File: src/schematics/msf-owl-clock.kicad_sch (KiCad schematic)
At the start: 38 parts, among them U001 BC805M

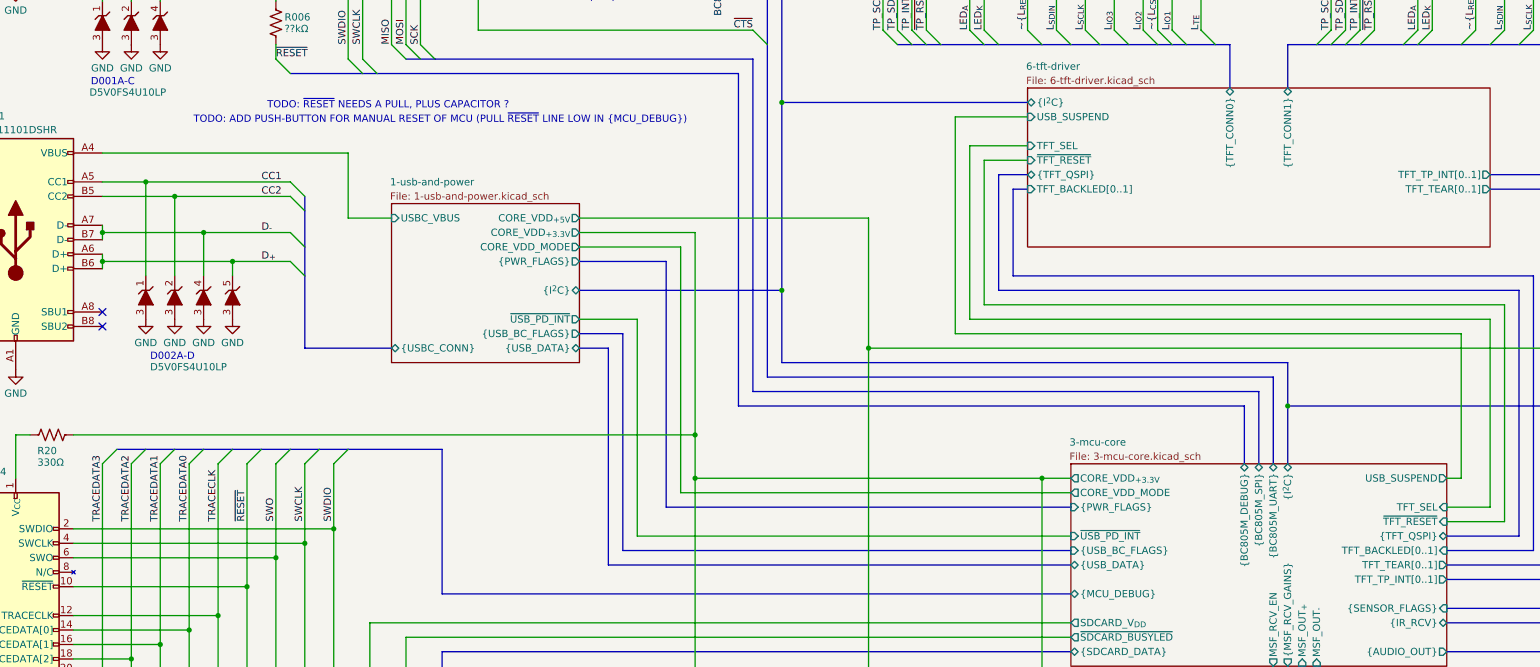
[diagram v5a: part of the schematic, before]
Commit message: Further elaboration of the USB / Power schematic.
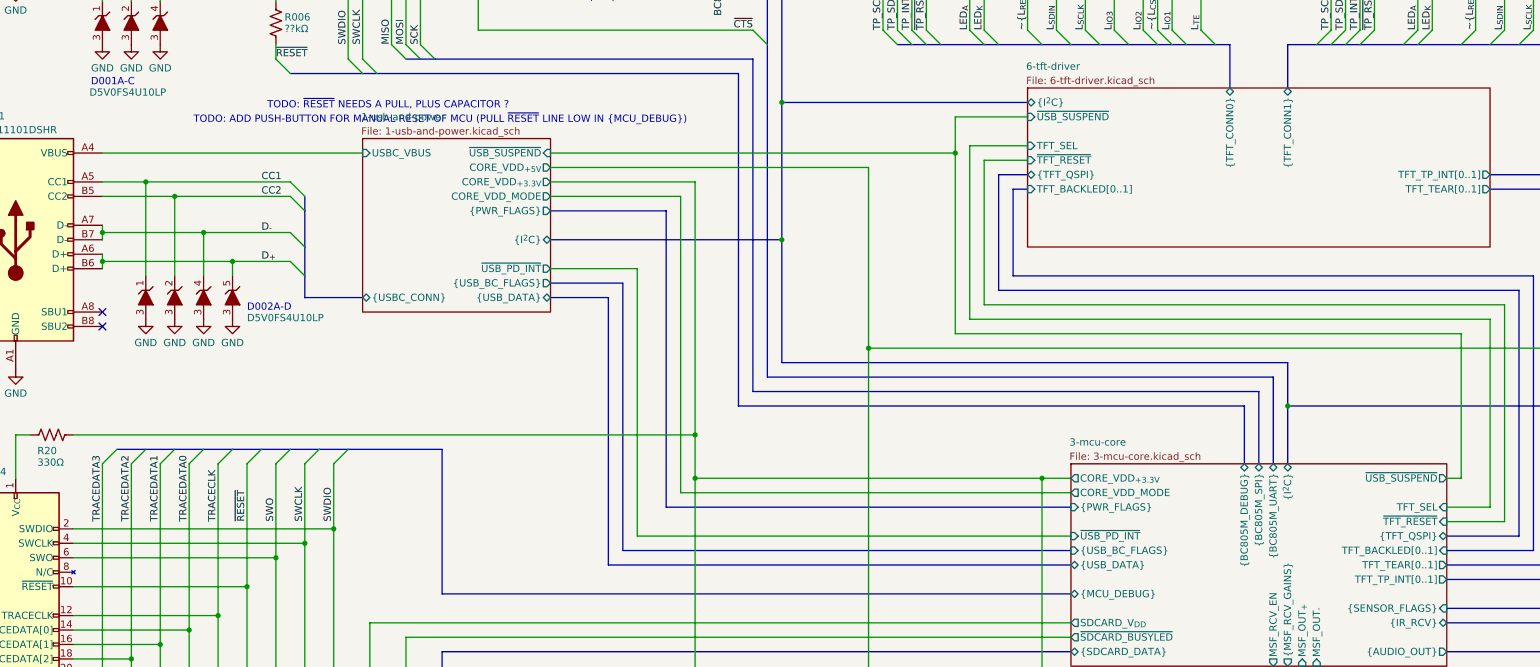
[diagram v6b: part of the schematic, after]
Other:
- sheet 1-usb-and-power ports: added ~{USB_SUSPEND}; removed none
- sheet 3-mcu-core ports: added ~{USB_SUSPEND}; removed USB_SUSPEND
- sheet 6-tft-driver ports: added ~{USB_SUSPEND}; removed USB_SUSPEND
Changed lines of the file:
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@@
   (bus_alias "TFT_CONN1" (members "TP_SCL" "TP_SDA" "TP_INT" "~{TP_{RST}}" "LED_{A}" "LED_{K}" "~{L_{RES}}" "L_{SDIN}" "L_{SCLK}" "L_{IO[1..3]}" "~{L_{CS}}" "L_{TE}"))
   (bus_alias "USBC_CONN" (members "CC[1..2]" "D_{+}" "D_{-}" "SBU[1..2]"))
-  (bus_alias "USB_BC_FLAGS" (members "~{CHARGING_ALLOWED}" "CHARGER_DETECTED" "~{NO_DATA}"))
+  (bus_alias "USB_BC_FLAGS" (members "~{CHARGING_ALLOWED}" "~{CHARGER_DETECTED}" "~{HAS_DATA}"))
   (junction (at 66.04 90.17) (diameter 0) (color 0 0 0 0)
   )
   (junction (at 73.66 163.83) (diameter 0) (color 0 0 0 0)
   )
+  (junction (at 172.72 97.79) (diameter 0) (color 0 0 0 0)
+  )
   (junction (at 81.28 215.9) (diameter 0) (color 0 0 0 0)
   )
@@
   (junction (at 58.42 35.56) (diameter 0) (color 0 0 0 0)
   )
-  (junction (at 172.72 106.68) (diameter 0) (color 0 0 0 0)
+  (junction (at 203.2 82.55) (diameter 0) (color 0 0 0 0)
   )
   (junction (at 187.96 116.84) (diameter 0) (color 0 0 0 0)
@@
     (stroke (width 0) (type default))
   )
-  (wire (pts (xy 53.34 82.55) (xy 96.52 82.55))
-    (stroke (width 0) (type default))
-  )
   (bus (pts (xy 113.03 208.28) (xy 113.03 213.36))
     (stroke (width 0) (type default))
@@
     (stroke (width 0) (type default))
   )
-  (bus (pts (xy 172.72 106.68) (xy 172.72 119.38))
-    (stroke (width 0) (type default))
-  )
   (wire (pts (xy 88.9 137.16) (xy 88.9 151.13))
     (stroke (width 0) (type default))
@@
     (stroke (width 0) (type default))
   )
+  (wire (pts (xy 203.2 82.55) (xy 203.2 76.2))
+    (stroke (width 0) (type default))
+  )
   (wire (pts (xy 96.52 33.02) (xy 127 33.02))
     (stroke (width 0) (type default))
@@
     (stroke (width 0) (type default))
   )
+  (bus (pts (xy 172.72 97.79) (xy 172.72 119.38))
+    (stroke (width 0) (type default))
+  )
   (wire (pts (xy 274.32 48.26) (xy 274.32 60.96))
     (stroke (width 0) (type default))
@@
     (stroke (width 0) (type default))
   )
+  (wire (pts (xy 132.08 82.55) (xy 203.2 82.55))
+    (stroke (width 0) (type default))
+  )
   (wire (pts (xy 83.82 137.16) (xy 83.82 153.67))
     (stroke (width 0) (type default))
@@
     (stroke (width 0) (type default))
   )
-  (wire (pts (xy 147.32 111.76) (xy 147.32 149.86))
+  (wire (pts (xy 147.32 102.87) (xy 147.32 149.86))
     (stroke (width 0) (type default))
   )
@@
     (stroke (width 0) (type default))
   )
-  (bus (pts (xy 172.72 73.66) (xy 172.72 106.68))
+  (bus (pts (xy 172.72 73.66) (xy 172.72 97.79))
     (stroke (width 0) (type default))
   )
@@
     (stroke (width 0) (type default))
   )
-  (wire (pts (xy 187.96 93.98) (xy 187.96 116.84))
+  (wire (pts (xy 187.96 85.09) (xy 187.96 116.84))
     (stroke (width 0) (type default))
   )
@@
     (stroke (width 0) (type default))
   )
-  (wire (pts (xy 154.94 142.24) (xy 154.94 99.06))
+  (wire (pts (xy 154.94 142.24) (xy 154.94 90.17))
     (stroke (width 0) (type default))
   )
@@
     (stroke (width 0) (type default))
   )
-  (bus (pts (xy 142.24 116.84) (xy 137.16 116.84))
+  (bus (pts (xy 142.24 107.95) (xy 132.08 107.95))
     (stroke (width 0) (type default))
   )
@@
     (stroke (width 0) (type default))
   )
-  (bus (pts (xy 142.24 154.94) (xy 142.24 116.84))
+  (bus (pts (xy 142.24 154.94) (xy 142.24 107.95))
     (stroke (width 0) (type default))
   )
@@
     (stroke (width 0) (type default))
   )
-  (bus (pts (xy 88.9 104.14) (xy 88.9 116.84))
-    (stroke (width 0) (type default))
-  )
   (wire (pts (xy 38.1 22.86) (xy 38.1 15.24))
     (stroke (width 0) (type default))
@@
     (stroke (width 0) (type default))
   )
-  (wire (pts (xy 137.16 96.52) (xy 157.48 96.52))
+  (wire (pts (xy 132.08 87.63) (xy 157.48 87.63))
     (stroke (width 0) (type default))
   )
@@
     (stroke (width 0) (type default))
   )
-  (wire (pts (xy 157.48 96.52) (xy 157.48 132.08))
+  (wire (pts (xy 157.48 87.63) (xy 157.48 132.08))
     (stroke (width 0) (type default))
   )
@@
     (stroke (width 0) (type default))
   )
-  (bus (pts (xy 137.16 106.68) (xy 172.72 106.68))
+  (bus (pts (xy 132.08 97.79) (xy 172.72 97.79))
     (stroke (width 0) (type default))
   )
@@
     (stroke (width 0) (type default))
   )
-  (bus (pts (xy 137.16 101.6) (xy 152.4 101.6))
+  (bus (pts (xy 132.08 92.71) (xy 152.4 92.71))
     (stroke (width 0) (type default))
   )
@@
     (stroke (width 0) (type default))
   )
+  (bus (pts (xy 88.9 104.14) (xy 88.9 107.95))
+    (stroke (width 0) (type default))
+  )
   (wire (pts (xy 167.64 60.96) (xy 119.38 60.96))
     (stroke (width 0) (type default))
@@
     (stroke (width 0) (type default))
   )
-  (wire (pts (xy 203.2 114.3) (xy 203.2 76.2))
+  (wire (pts (xy 203.2 114.3) (xy 203.2 82.55))
     (stroke (width 0) (type default))
   )
@@
     (stroke (width 0) (type default))
   )
-  (bus (pts (xy 137.16 114.3) (xy 144.78 114.3))
+  (bus (pts (xy 132.08 105.41) (xy 144.78 105.41))
     (stroke (width 0) (type default))
   )
@@
     (stroke (width 0) (type default))
   )
-  (wire (pts (xy 96.52 93.98) (xy 104.14 93.98))
+  (wire (pts (xy 53.34 82.55) (xy 99.06 82.55))
     (stroke (width 0) (type default))
   )
@@
     (stroke (width 0) (type default))
   )
-  (wire (pts (xy 96.52 82.55) (xy 96.52 93.98))
-    (stroke (width 0) (type default))
-  )
   (bus (pts (xy 113.03 160.02) (xy 113.03 134.62))
     (stroke (width 0) (type default))
@@
     (stroke (width 0) (type default))
   )
-  (wire (pts (xy 137.16 111.76) (xy 147.32 111.76))
+  (wire (pts (xy 132.08 102.87) (xy 147.32 102.87))
     (stroke (width 0) (type default))
   )
-  (wire (pts (xy 137.16 93.98) (xy 187.96 93.98))
+  (wire (pts (xy 132.08 85.09) (xy 187.96 85.09))
     (stroke (width 0) (type default))
   )
@@
     (stroke (width 0) (type default))
   )
-  (bus (pts (xy 144.78 152.4) (xy 144.78 114.3))
+  (bus (pts (xy 144.78 152.4) (xy 144.78 105.41))
     (stroke (width 0) (type default))
   )
@@
     (stroke (width 0) (type default))
   )
-  (bus (pts (xy 88.9 116.84) (xy 104.14 116.84))
+  (bus (pts (xy 88.9 107.95) (xy 99.06 107.95))
     (stroke (width 0) (type default))
   )
@@
     (stroke (width 0) (type default))
   )
-  (wire (pts (xy 154.94 99.06) (xy 137.16 99.06))
+  (wire (pts (xy 154.94 90.17) (xy 132.08 90.17))
     (stroke (width 0) (type default))
   )
@@
     (stroke (width 0) (type default))
   )
-  (bus (pts (xy 152.4 101.6) (xy 152.4 144.78))
+  (bus (pts (xy 152.4 92.71) (xy 152.4 144.78))
     (stroke (width 0) (type default))
   )
@@
     (effects (font (size 1.27 1.27)) (justify left bottom))
   )
-  (text "D002A-D" (at 61.722 119.126 0)
+  (text "D002A-D" (at 78.74 110.49 0)
     (effects (font (size 1.27 1.27)) (justify left bottom))
   )
@@
       (effects (font (size 1.27 1.27)) (justify right) hide)
     )
-    (property "Value" "D5V0FS4U10LP" (at 61.722 120.142 90)
+    (property "Value" "D5V0FS4U10LP" (at 78.74 111.506 90)
       (effects (font (size 1.27 1.27)) (justify right))
     )
@@
       (effects (font (size 1.27 1.27)) (justify right))
     )
-    (pin "USB_SUSPEND" input (at 215.9 76.2 180)
+    (pin "~{USB_SUSPEND}" input (at 215.9 76.2 180)
       (effects (font (size 1.27 1.27)) (justify left))
     )
@@
     )
   )
-  (sheet (at 104.14 91.44) (size 33.02 27.94)
+  (sheet (at 99.06 80.01) (size 33.02 30.48)
     (stroke (width 0.1524) (type solid))
     (fill (color 0 0 0 0.0000))
-    (property "Sheetname" "1-usb-and-power" (at 103.886 88.392 0)
+    (property "Sheetname" "1-usb-and-power" (at 98.806 76.962 0)
       (effects (font (size 1.27 1.27)) (justify left bottom))
     )
-    (property "Sheetfile" "1-usb-and-power.kicad_sch" (at 103.886 89.408 0)
+    (property "Sheetfile" "1-usb-and-power.kicad_sch" (at 98.806 77.978 0)
       (effects (font (size 1.27 1.27)) (justify left top))
     )
-    (pin "{I^{2}C}" bidirectional (at 137.16 106.68 0)
+    (pin "{I^{2}C}" bidirectional (at 132.08 97.79 0)
       (effects (font (size 1.27 1.27)) (justify right))
     )
-    (pin "{USBC_CONN}" bidirectional (at 104.14 116.84 180)
+    (pin "{USBC_CONN}" bidirectional (at 99.06 107.95 180)
       (effects (font (size 1.27 1.27)) (justify left))
     )
-    (pin "USBC_VBUS" input (at 104.14 93.98 180)
+    (pin "USBC_VBUS" input (at 99.06 82.55 180)
       (effects (font (size 1.27 1.27)) (justify left))
     )
-    (pin "{USB_DATA}" bidirectional (at 137.16 116.84 0)
+    (pin "{USB_DATA}" bidirectional (at 132.08 107.95 0)
+      (effects (font (size 1.27 1.27)) (justify right))
+    )
+    (pin "{PWR_FLAGS}" output (at 132.08 92.71 0)
       (effects (font (size 1.27 1.27)) (justify right))
     )
-    (pin "{PWR_FLAGS}" output (at 137.16 101.6 0)
+    (pin "~{USB_PD_INT}" output (at 132.08 102.87 0)
       (effects (font (size 1.27 1.27)) (justify right))
     )
-    (pin "~{USB_PD_INT}" output (at 137.16 111.76 0)
+    (pin "{USB_BC_FLAGS}" output (at 132.08 105.41 0)
       (effects (font (size 1.27 1.27)) (justify right))
     )
-    (pin "{USB_BC_FLAGS}" output (at 137.16 114.3 0)
+    (pin "CORE_VDD_{+3.3V}" output (at 132.08 87.63 0)
       (effects (font (size 1.27 1.27)) (justify right))
     )
-    (pin "CORE_VDD_{+3.3V}" output (at 137.16 96.52 0)
+    (pin "CORE_VDD_{+5V}" output (at 132.08 85.09 0)
       (effects (font (size 1.27 1.27)) (justify right))
     )
-    (pin "CORE_VDD_{+5V}" output (at 137.16 93.98 0)
+    (pin "CORE_VDD_MODE" output (at 132.08 90.17 0)
       (effects (font (size 1.27 1.27)) (justify right))
     )
-    (pin "CORE_VDD_MODE" output (at 137.16 99.06 0)
+    (pin "~{USB_SUSPEND}" input (at 132.08 82.55 0)
       (effects (font (size 1.27 1.27)) (justify right))
     )
@@
       (effects (font (size 1.27 1.27)) (justify left))
     )
-    (pin "USB_SUSPEND" output (at 289.56 139.7 0)
+    (pin "~{USB_SUSPEND}" output (at 289.56 139.7 0)
       (effects (font (size 1.27 1.27)) (justify right))
     )
